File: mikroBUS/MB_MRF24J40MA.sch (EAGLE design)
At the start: 2 parts

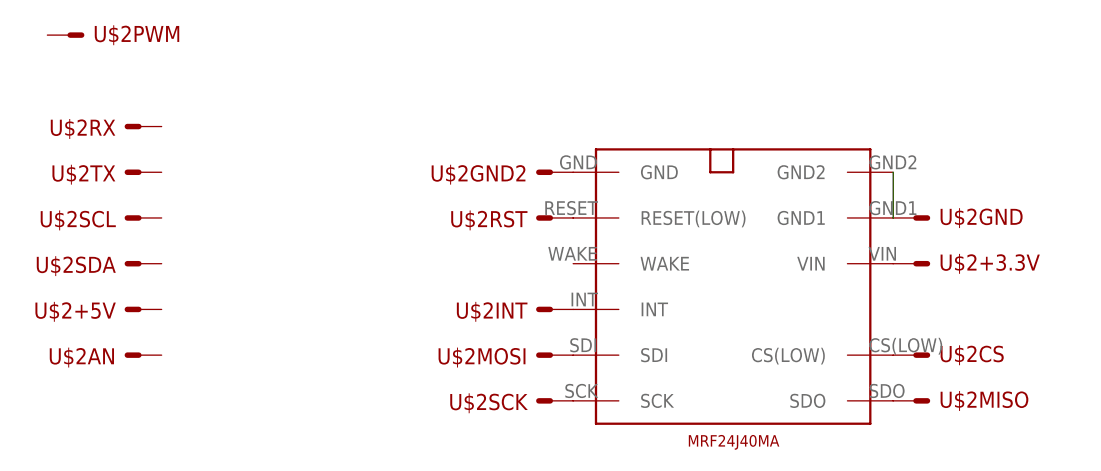
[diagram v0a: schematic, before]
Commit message: 
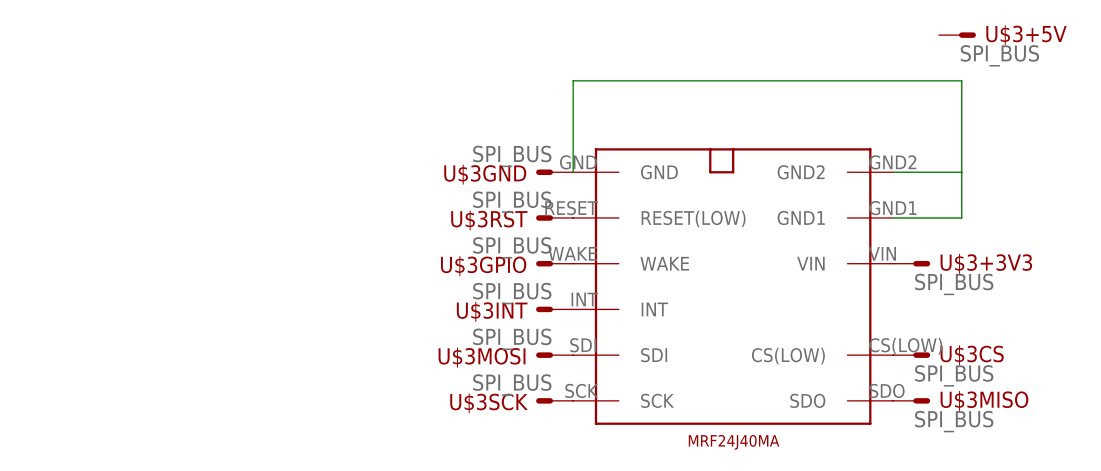
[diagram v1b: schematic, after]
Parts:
- removed U$2: (no value), lieven:MIKROBUSSIL
- added U$3: SPI_BUS, lieven:SPI_BUS
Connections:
- net N$1: now also U$1.GND, U$1.GND1, U$1.GND2, U$3GND.S; no longer U$1.INT, U$2INT.S
- net N$2: now also U$1.VIN, U$3+3V3.S; no longer U$1.GND, U$2GND2.S
- net N$3: now also U$1.SDI, U$3MOSI.S; no longer U$1.RESET(LOW), U$2RST.S
- net N$4: now also U$1.SDO, U$3MISO.S; no longer U$1.CS(LOW), U$2CS.S
- net N$5: now also U$3SCK.S; no longer U$2SCK.S
- net N$6: now also U$1.CS(LOW), U$3CS.S; no longer U$1.SDO, U$2MISO.S
- net N$7: now also U$1.INT, U$3INT.S; no longer U$1.SDI, U$2MOSI.S
- net N$8: now also U$1.RESET(LOW), U$3RST.S; no longer U$1.VIN, U$2+3.3V.S
- net N$9: now also U$1.WAKE, U$3GPIO.S; no longer U$1.GND1, U$1.GND2, U$2GND.S
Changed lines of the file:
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@@
 <parts>
 <part name="U$1" library="lieven" deviceset="MRF24J40MA" device=""/>
-<part name="U$2" library="lieven" deviceset="MIKROBUS" device="SIL"/>
+<part name="U$3" library="lieven" deviceset="SPI_BUS" device=""/>
 </parts>
 <sheets>
@@
 <instances>
 <instance part="U$1" gate="G$1" x="76.2" y="53.34"/>
-<instance part="U$2" gate="PWM" x="-5.08" y="73.66"/>
-<instance part="U$2" gate="INT" x="48.26" y="43.18" rot="R180"/>
-<instance part="U$2" gate="RX" x="2.54" y="63.5" rot="R180"/>
-<instance part="U$2" gate="TX" x="2.54" y="58.42" rot="R180"/>
-<instance part="U$2" gate="SCL" x="2.54" y="53.34" rot="R180"/>
-<instance part="U$2" gate="SDA" x="2.54" y="48.26" rot="R180"/>
-<instance part="U$2" gate="+5V" x="2.54" y="43.18" rot="R180"/>
-<instance part="U$2" gate="GND2" x="48.26" y="58.42" rot="R180"/>
-<instance part="U$2" gate="AN" x="2.54" y="38.1" rot="R180"/>
-<instance part="U$2" gate="RST" x="48.26" y="53.34" rot="R180"/>
-<instance part="U$2" gate="CS" x="88.9" y="38.1"/>
-<instance part="U$2" gate="SCK" x="48.26" y="33.02" rot="R180"/>
-<instance part="U$2" gate="MISO" x="88.9" y="33.02"/>
-<instance part="U$2" gate="MOSI" x="48.26" y="38.1" rot="R180"/>
-<instance part="U$2" gate="+3.3V" x="88.9" y="48.26"/>
-<instance part="U$2" gate="GND" x="88.9" y="53.34"/>
+<instance part="U$3" gate="GND" x="48.26" y="58.42" rot="R180"/>
+<instance part="U$3" gate="+3V3" x="88.9" y="48.26"/>
+<instance part="U$3" gate="+5V" x="93.98" y="73.66"/>
+<instance part="U$3" gate="MOSI" x="48.26" y="38.1" rot="R180"/>
+<instance part="U$3" gate="MISO" x="88.9" y="33.02"/>
+<instance part="U$3" gate="SCK" x="48.26" y="33.02" rot="R180"/>
+<instance part="U$3" gate="CS" x="88.9" y="38.1"/>
+<instance part="U$3" gate="INT" x="48.26" y="43.18" rot="R180"/>
+<instance part="U$3" gate="RST" x="48.26" y="53.34" rot="R180"/>
+<instance part="U$3" gate="GPIO" x="48.26" y="48.26" rot="R180"/>
 </instances>
 <busses>
@@
 <net name="N$1" class="0">
 <segment>
-<pinref part="U$1" gate="G$1" pin="INT"/>
-<pinref part="U$2" gate="INT" pin="S"/>
+<pinref part="U$1" gate="G$1" pin="GND"/>
+<pinref part="U$3" gate="GND" pin="S"/>
+<wire x1="50.8" y1="58.42" x2="50.8" y2="68.58" width="0.1524" layer="91"/>
+<wire x1="50.8" y1="68.58" x2="93.98" y2="68.58" width="0.1524" layer="91"/>
+<wire x1="93.98" y1="68.58" x2="93.98" y2="58.42" width="0.1524" layer="91"/>
+<pinref part="U$1" gate="G$1" pin="GND2"/>
+<wire x1="93.98" y1="58.42" x2="86.36" y2="58.42" width="0.1524" layer="91"/>
+<pinref part="U$1" gate="G$1" pin="GND1"/>
+<wire x1="86.36" y1="53.34" x2="93.98" y2="53.34" width="0.1524" layer="91"/>
+<wire x1="93.98" y1="53.34" x2="93.98" y2="58.42" width="0.1524" layer="91"/>
 </segment>
 </net>
 <net name="N$2" class="0">
 <segment>
-<pinref part="U$1" gate="G$1" pin="GND"/>
-<pinref part="U$2" gate="GND2" pin="S"/>
+<pinref part="U$1" gate="G$1" pin="VIN"/>
+<pinref part="U$3" gate="+3V3" pin="S"/>
 </segment>
 </net>
 <net name="N$3" class="0">
 <segment>
-<pinref part="U$1" gate="G$1" pin="RESET(LOW)"/>
-<pinref part="U$2" gate="RST" pin="S"/>
+<pinref part="U$1" gate="G$1" pin="SDI"/>
+<pinref part="U$3" gate="MOSI" pin="S"/>
 </segment>
 </net>
 <net name="N$4" class="0">
 <segment>
-<pinref part="U$1" gate="G$1" pin="CS(LOW)"/>
-<pinref part="U$2" gate="CS" pin="S"/>
+<pinref part="U$1" gate="G$1" pin="SDO"/>
+<pinref part="U$3" gate="MISO" pin="S"/>
 </segment>
 </net>
@@
 <segment>
 <pinref part="U$1" gate="G$1" pin="SCK"/>
-<pinref part="U$2" gate="SCK" pin="S"/>
+<pinref part="U$3" gate="SCK" pin="S"/>
 </segment>
 </net>
 <net name="N$6" class="0">
 <segment>
-<pinref part="U$1" gate="G$1" pin="SDO"/>
-<pinref part="U$2" gate="MISO" pin="S"/>
+<pinref part="U$1" gate="G$1" pin="CS(LOW)"/>
+<pinref part="U$3" gate="CS" pin="S"/>
 </segment>
 </net>
 <net name="N$7" class="0">
 <segment>
-<pinref part="U$1" gate="G$1" pin="SDI"/>
-<pinref part="U$2" gate="MOSI" pin="S"/>
+<pinref part="U$1" gate="G$1" pin="INT"/>
+<pinref part="U$3" gate="INT" pin="S"/>
 </segment>
 </net>
 <net name="N$8" class="0">
 <segment>
-<pinref part="U$1" gate="G$1" pin="VIN"/>
-<pinref part="U$2" gate="+3.3V" pin="S"/>
+<pinref part="U$1" gate="G$1" pin="RESET(LOW)"/>
+<pinref part="U$3" gate="RST" pin="S"/>
 </segment>
 </net>
 <net name="N$9" class="0">
 <segment>
-<pinref part="U$1" gate="G$1" pin="GND1"/>
-<pinref part="U$2" gate="GND" pin="S"/>
-<pinref part="U$1" gate="G$1" pin="GND2"/>
-<wire x1="86.36" y1="58.42" x2="86.36" y2="53.34" width="0.1524" layer="91"/>
+<pinref part="U$1" gate="G$1" pin="WAKE"/>
+<pinref part="U$3" gate="GPIO" pin="S"/>
 </segment>
 </net>
